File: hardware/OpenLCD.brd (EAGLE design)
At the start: 45.7 x 30.5 mm, 42 parts, among them Q1 PNP-500mA, Q2 PNP-500mA, Q3 PNP-500mA, U1 ATMEGA328P_TQFP, U2 4BIT-RGB, U3 MIC5205-ADJ, Y2 8MHz

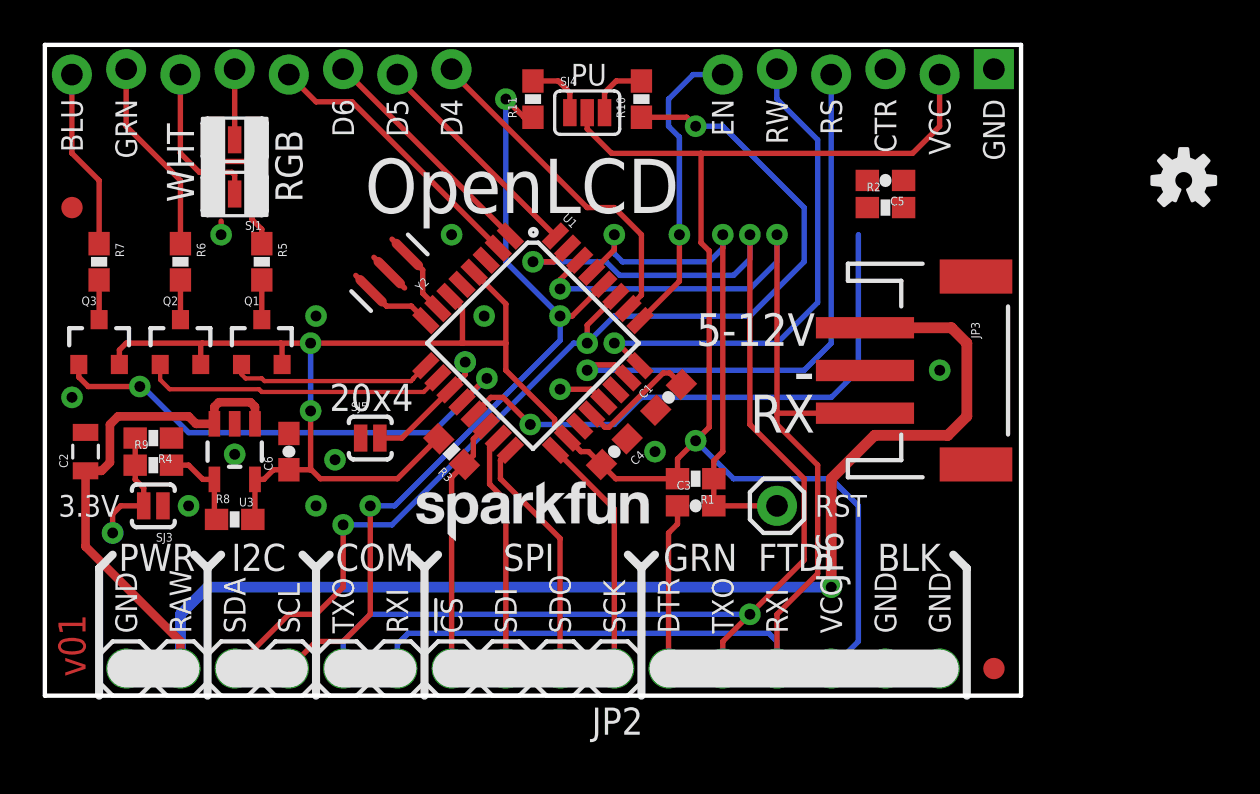
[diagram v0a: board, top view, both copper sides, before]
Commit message: Add back contrast trimpot. Add Bypass jumper.
Software contrast control is unreliable on too many types of LCDs.
Returned to a trimpot. Added a bypass jumper to allow for LCDs with
larger backlight requirements.
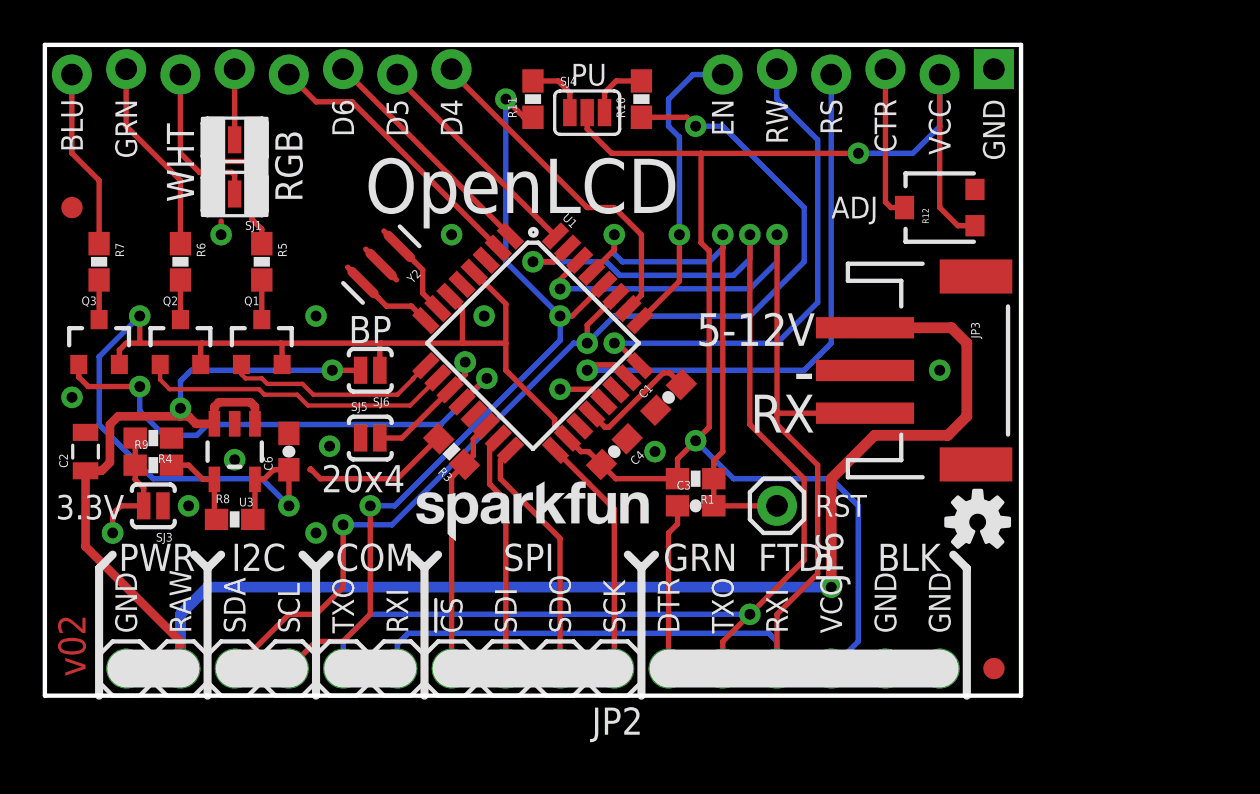
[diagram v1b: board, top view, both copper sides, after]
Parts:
- removed C5: 0.1uF, SparkFun-Capacitors:0603-CAP
- removed R2: 220, SparkFun-Resistors:0603-RES
- added R12: 10k, SparkFun-Electromechanical:TRIMPOT-3MM
- added SJ6: Bypass, SparkFun-Passives:PAD-JUMPER-2-NO_YES_SILK
- moved U$4 18.7 mm to (43.7, 8.13)
- moved Y2 0.54 mm to (15.7, 20.2)
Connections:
- net N$7 renamed 3.3V_CTRL
- removed net FILTERED_CONTRAST: C5.2, R2.1, U2.3
- new net N$8: R12.2, U2.3
- net CONTRAST: no longer R2.2
- net GND: now also R12.3; no longer C5.1
- net RAW: now also SJ6.2
- net VCC: now also R12.1, SJ6.1
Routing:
- net CONTRAST: track 26.2 -> 0.00 mm, vias 1 -> 0
- net VCC: track 110.2 -> 132.2 mm, vias 3 -> 4
- net RAW: track 77.7 -> 88.0 mm, vias 1 -> 3
- net N$8: track 0.00 -> 7.23 mm
- net BL-B: track 23.4 -> 24.2 mm
- net N$3: track 2.11 -> 2.65 mm
- net N$2: track 2.13 -> 2.67 mm
- net BL-R/W: track 9.54 -> 10.1 mm
- net BL-G: track 14.2 -> 14.8 mm
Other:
- board text added: "ADJ"
- board text added: "BP"
- board text added: "v02"
- board text removed: "v01"
